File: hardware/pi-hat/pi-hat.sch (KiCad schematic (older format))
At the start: 75 parts, among them J1 PWR IN, J10 6-8, J11 PWM0, J12 PWM1, J13 KLPX-0848A-2-B, J14 KLPX-0848A-2-R, J2 A-F, J3 40HAT, J4 G-M, J5 N-Q, J6 PANEL_PWR, J7 PANEL_CTL, J8 2-5, J9 WP, Q1 DMG2305UX, Q2 DMMT5401, Q3 DMN6075S, Q4 NTR4171P, U1 CAT24C32, U10 L78L33_SOT89, U11 L78L33_SOT89, U12 PCM5122PW, U2 CM1293A, U3 CM1293A, U4 CM1293A, U5 CM1293A, U6 CM1293A, U7 CM1293A, U8 MCP23S17_SO, U9 MCP23S17_SO

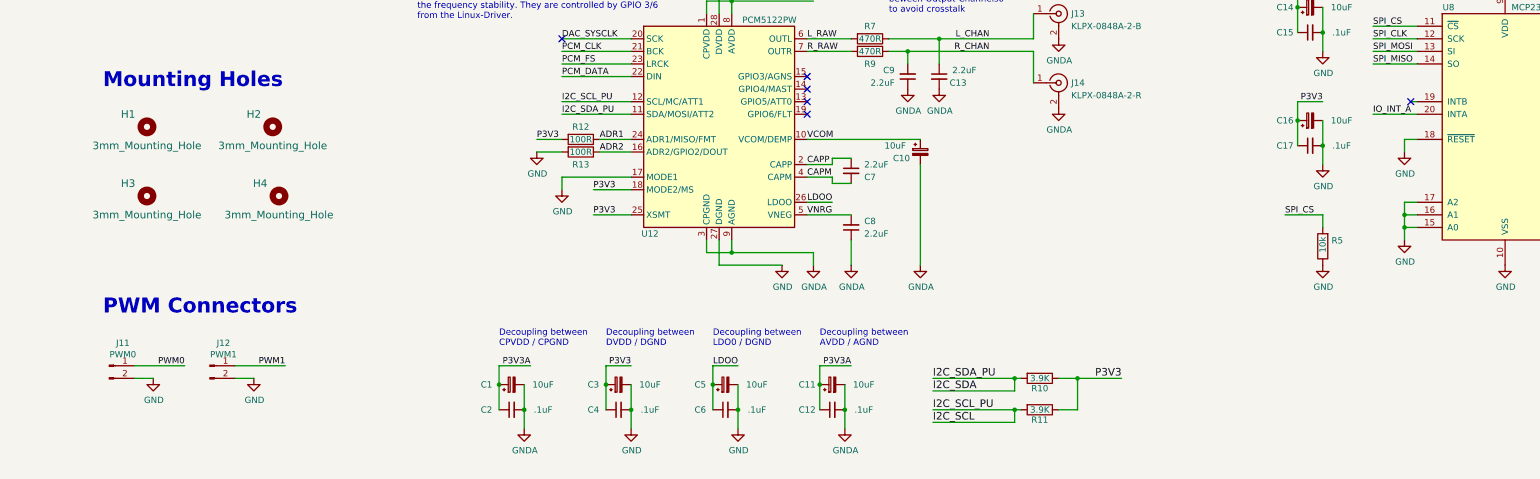
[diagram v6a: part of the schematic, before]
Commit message: fully routed
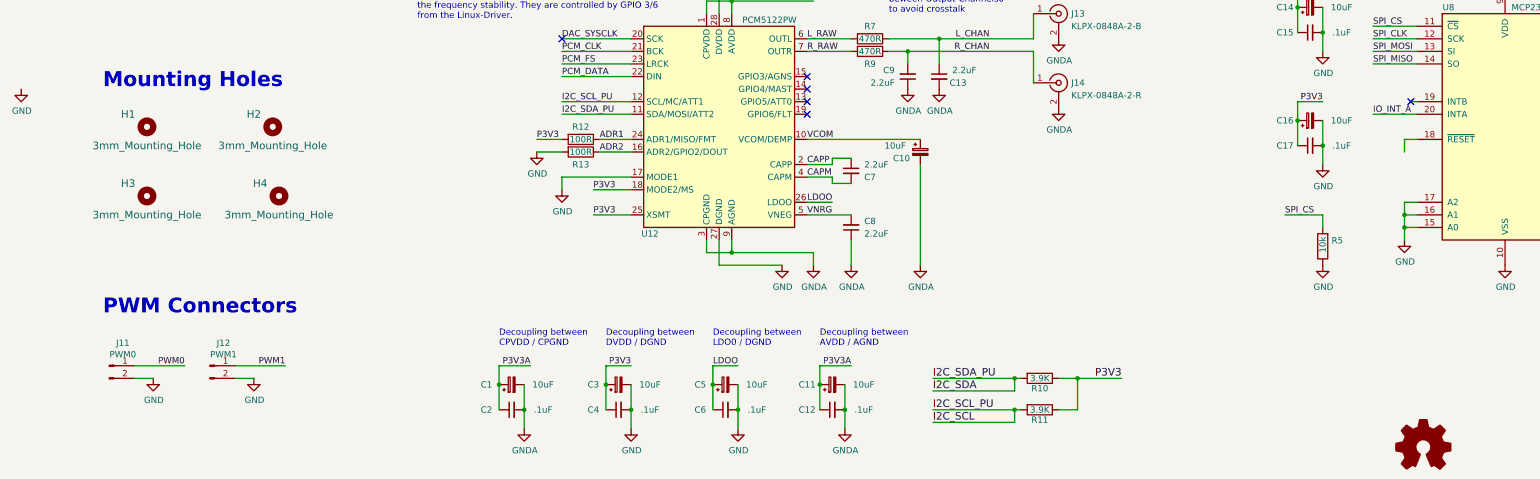
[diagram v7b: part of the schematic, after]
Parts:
- JP1: footprint Jumper:SolderJumper-2_P1.3mm_Bridged2Bar_RoundedPad1.0x1.5mm -> NetTie:NetTie-2_SMD_Pad0.5mm
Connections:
- net GND: no longer U8.18 (~RESET~)
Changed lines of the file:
@@
 L power:GND #PWR018
 U 1 1 5ED9D663
-P 11400 8650
-F 0 "#PWR018" H 11400 8400 50  0001 C CNN
-F 1 "GND" H 11405 8477 50  0000 C CNN
-F 2 "" H 11400 8650 50  0001 C CNN
-F 3 "" H 11400 8650 50  0001 C CNN
-	1    11400 8650
+P 400 8150
+F 0 "#PWR018" H 400 7900 50  0001 C CNN
+F 1 "GND" H 405 7977 50  0000 C CNN
+F 2 "" H 400 8150 50  0001 C CNN
+F 3 "" H 400 8150 50  0001 C CNN
+	1    400  8150
 	1    0    0    -1
 $EndComp
@@
 F 0 "JP1" H 9250 4421 50  0001 C CNN
 F 1 "Jumper_NC_Small" H 9250 4421 50  0001 C CNN
-F 2 "Jumper:SolderJumper-2_P1.3mm_Bridged2Bar_RoundedPad1.0x1.5mm" H 9250 4300 50  0001 C CNN
+F 2 "NetTie:NetTie-2_SMD_Pad0.5mm" H 9250 4300 50  0001 C CNN
 F 3 "~" H 9250 4300 50  0001 C CNN
 	1    9250 4300
@@
 	12550 2300 14800 2300
 Connection ~ 12550 2500
+$Comp
+L Graphic:Logo_Open_Hardware_Small #LOGO1
+U 1 1 5E8DC3DA
+P 11550 11000
+F 0 "#LOGO1" H 11550 11500 50  0001 C CNN
+F 1 "Logo_Open_Hardware_Large" H 11550 10600 50  0001 C CNN
+F 2 "Symbol:OSHW-Logo2_7.3x6mm_SilkScreen" H 11550 11000 50  0001 C CNN
+F 3 "~" H 11550 11000 50  0001 C CNN
+	1    11550 11000
+	1    0    0    -1
+$EndComp
 $EndSCHEMATC

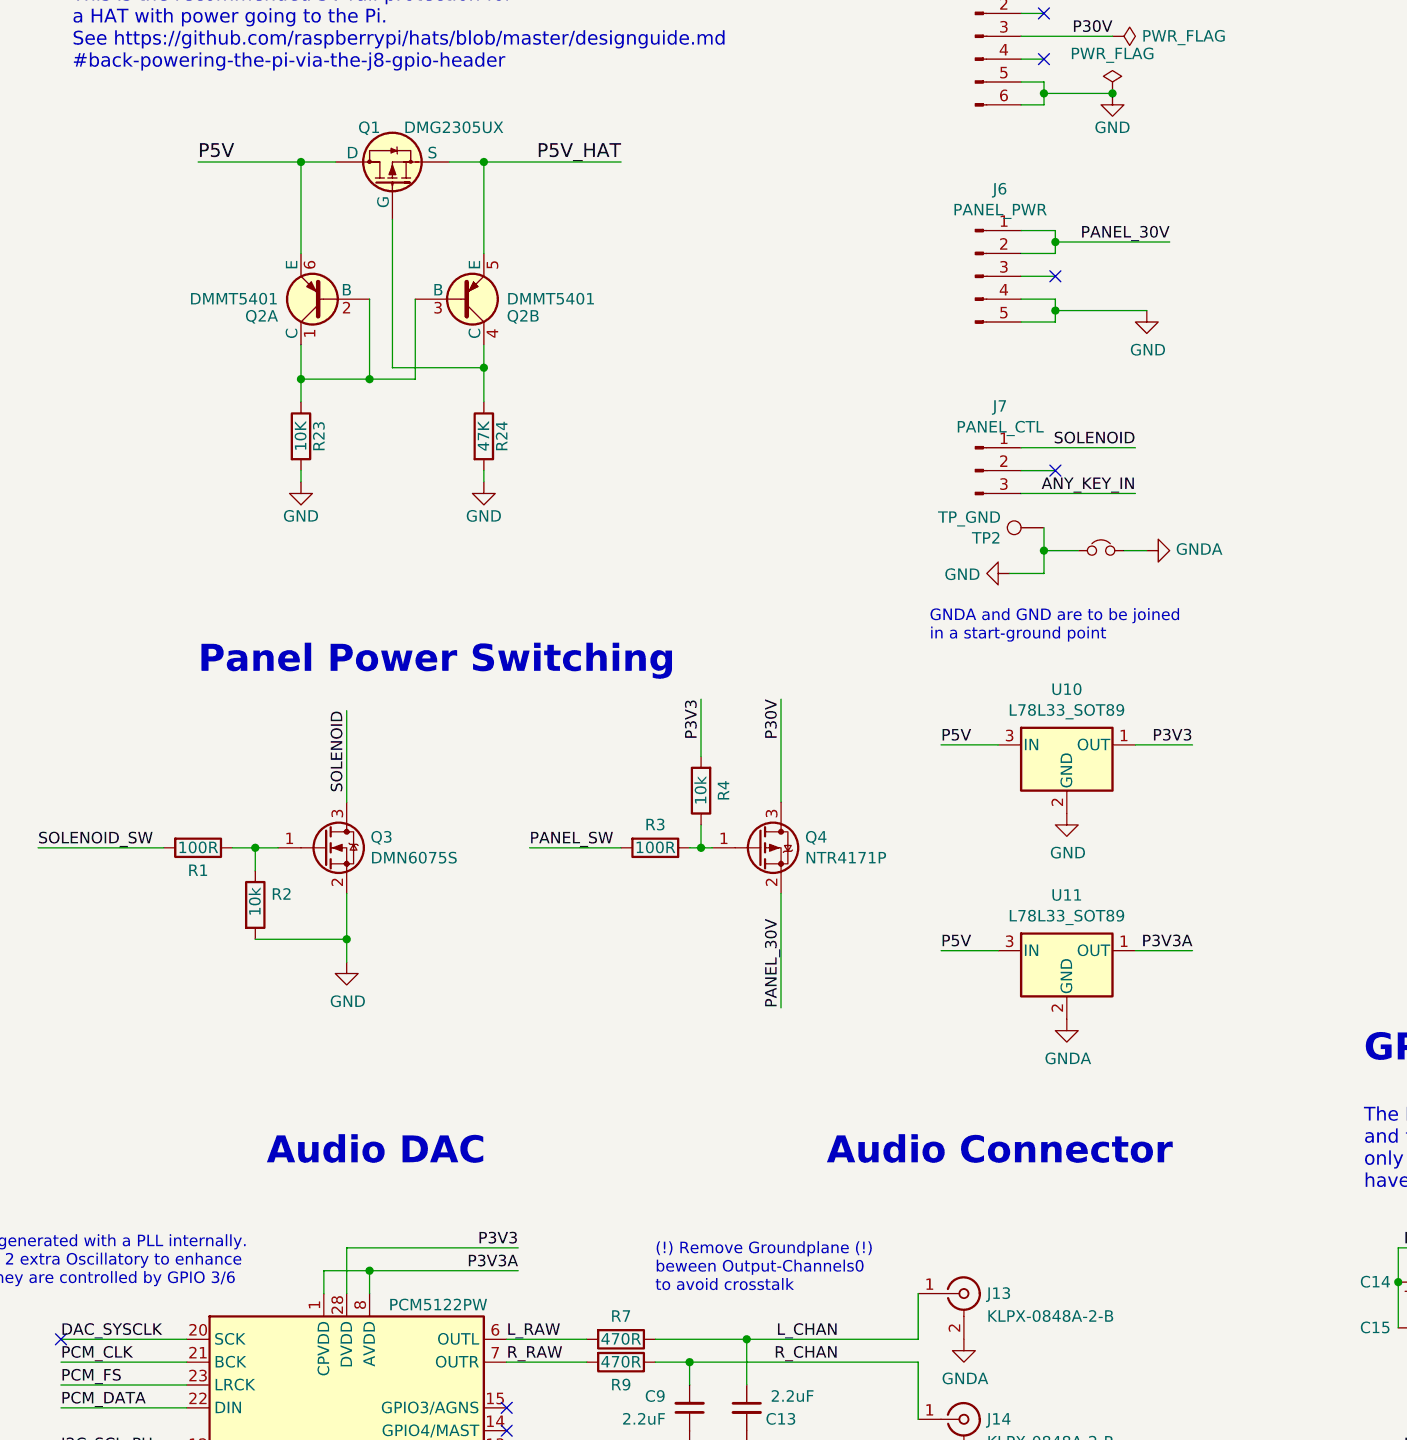
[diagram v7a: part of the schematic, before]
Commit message: add icons and voltage testpoints
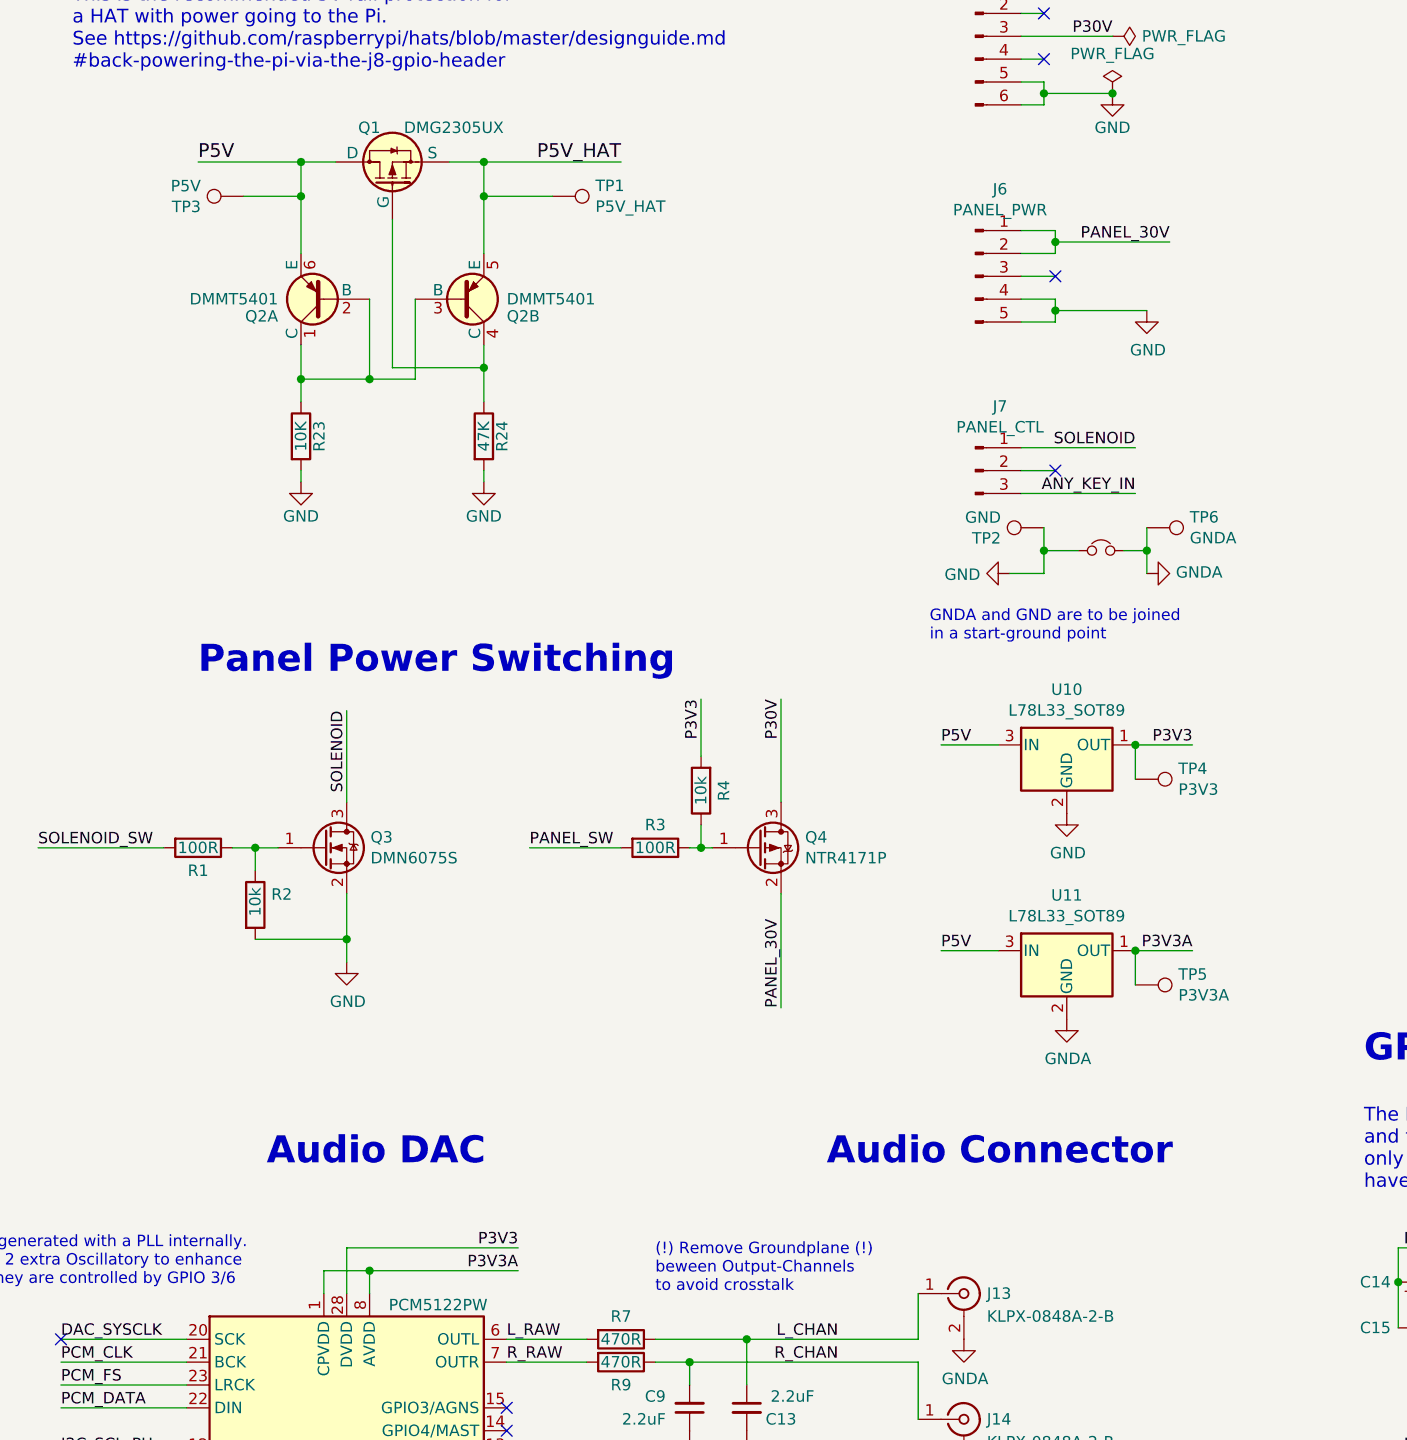
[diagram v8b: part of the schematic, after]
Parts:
- added OSHW1: Logo_Open_Hardware_Large, Symbol:OSHW-Logo2_7.3x6mm_SilkScreen, symbol Graphic:Logo_Open_Hardware_Small
- added TP1: P5V_HAT, TestPoint:TestPoint_Pad_D2.0mm, symbol Connector:TestPoint
- added TP3: P5V, TestPoint:TestPoint_Pad_D2.0mm, symbol Connector:TestPoint
- added TP4: P3V3, TestPoint:TestPoint_Pad_D2.0mm, symbol Connector:TestPoint
- added TP5: P3V3A, TestPoint:TestPoint_Pad_D2.0mm, symbol Connector:TestPoint
- added TP6: GNDA, TestPoint:TestPoint_Pad_D2.0mm, symbol Connector:TestPoint
- TP2: value TP_GND -> GND
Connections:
- net GNDA: now also TP6.1
- net P3V3: now also TP4.1
- net P3V3A: now also TP5.1
- net P5V: now also TP3.1
- net P5V_HAT: now also TP1.1
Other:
- note added: "(!) Remove Groundplane (!)\nbeween Output-Channels\nto avoid crosstalk"
- note removed: "(!) Remove Groundplane (!)\nbeween Output-Channels0\nto avoid crosstalk"
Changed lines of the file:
@@
 $EndComp
-Wire Wire Line
-	8900 1850 9300 1850
 Wire Wire Line
 	8900 1950 9000 1950
@@
 Connection ~ 6550 2600
 Wire Wire Line
-	6550 3000 6550 2600
+	6550 3000 6550 2750
 Connection ~ 5750 2600
 Wire Wire Line
-	5750 3000 5750 2600
+	5750 3000 5750 2750
 Connection ~ 6050 3550
 Wire Wire Line
@@
 P 9000 4200
 F 0 "TP2" V 8954 4388 50  0000 L CNN
-F 1 "TP_GND" V 9045 4388 50  0000 L CNN
+F 1 "GND" V 9045 4388 50  0000 L CNN
 F 2 "TestPoint:TestPoint_Pad_D2.0mm" H 9200 4200 50  0001 C CNN
 F 3 "~" H 9200 4200 50  0001 C CNN
@@
 L power:GNDA #PWR0106
 U 1 1 6024E074
-P 9450 4300
-F 0 "#PWR0106" H 9450 4050 50  0001 C CNN
-F 1 "GNDA" V 9455 4173 50  0000 R CNN
-F 2 "" H 9450 4300 50  0001 C CNN
-F 3 "" H 9450 4300 50  0001 C CNN
-	1    9450 4300
+P 9450 4400
+F 0 "#PWR0106" H 9450 4150 50  0001 C CNN
+F 1 "GNDA" V 9455 4273 50  0000 R CNN
+F 2 "" H 9450 4400 50  0001 C CNN
+F 3 "" H 9450 4400 50  0001 C CNN
+	1    9450 4400
 	0    -1   -1   0
 $EndComp
@@
 $EndComp
 Text Notes 7300 7550 0    50   ~ 0
-(!) Remove Groundplane (!)\nbeween Output-Channels0\nto avoid crosstalk
+(!) Remove Groundplane (!)\nbeween Output-Channels\nto avoid crosstalk
 Wire Wire Line
 	10750 9250 10750 9150
@@
 Connection ~ 12550 2500
 $Comp
-L Graphic:Logo_Open_Hardware_Small #LOGO1
+L Graphic:Logo_Open_Hardware_Small OSHW1
 U 1 1 5E8DC3DA
 P 11550 11000
-F 0 "#LOGO1" H 11550 11500 50  0001 C CNN
+F 0 "OSHW1" H 11550 11500 50  0001 C CNN
 F 1 "Logo_Open_Hardware_Large" H 11550 10600 50  0001 C CNN
 F 2 "Symbol:OSHW-Logo2_7.3x6mm_SilkScreen" H 11550 11000 50  0001 C CNN
@@
 	1    0    0    -1
 $EndComp
+$Comp
+L Connector:TestPoint TP3
+U 1 1 5EA57104
+P 5500 2750
+F 0 "TP3" V 5454 2938 50  0000 L CNN
+F 1 "P5V" V 5545 2938 50  0000 L CNN
+F 2 "TestPoint:TestPoint_Pad_D2.0mm" H 5700 2750 50  0001 C CNN
+F 3 "~" H 5700 2750 50  0001 C CNN
+	1    5500 2750
+	0    -1   -1   0
+$EndComp
+$Comp
+L Connector:TestPoint TP1
+U 1 1 5EA97686
+P 6850 2750
+F 0 "TP1" V 6804 2938 50  0000 L CNN
+F 1 "P5V_HAT" V 6895 2938 50  0000 L CNN
+F 2 "TestPoint:TestPoint_Pad_D2.0mm" H 7050 2750 50  0001 C CNN
+F 3 "~" H 7050 2750 50  0001 C CNN
+	1    6850 2750
+	0    1    1    0
+$EndComp
+Wire Wire Line
+	6850 2750 6550 2750
+Connection ~ 6550 2750
+Wire Wire Line
+	6550 2750 6550 2600
+$Comp
+L Connector:TestPoint TP4
+U 1 1 5EACB533
+P 9400 5300
+F 0 "TP4" V 9354 5488 50  0000 L CNN
+F 1 "P3V3" V 9445 5488 50  0000 L CNN
+F 2 "TestPoint:TestPoint_Pad_D2.0mm" H 9600 5300 50  0001 C CNN
+F 3 "~" H 9600 5300 50  0001 C CNN
+	1    9400 5300
+	0    1    1    0
+$EndComp
+$Comp
+L Connector:TestPoint TP5
+U 1 1 5EACDD2D
+P 9400 6200
+F 0 "TP5" V 9354 6388 50  0000 L CNN
+F 1 "P3V3A" V 9445 6388 50  0000 L CNN
+F 2 "TestPoint:TestPoint_Pad_D2.0mm" H 9600 6200 50  0001 C CNN
+F 3 "~" H 9600 6200 50  0001 C CNN
+	1    9400 6200
+	0    1    1    0
+$EndComp
+Wire Wire Line
+	9400 6200 9400 6050
+Connection ~ 9400 6050
+Wire Wire Line
+	9400 5300 9400 5150
+Connection ~ 9400 5150
+$Comp
+L Connector:TestPoint TP6
+U 1 1 5EB41904
+P 9450 4200
+F 0 "TP6" V 9404 4388 50  0000 L CNN
+F 1 "GNDA" V 9495 4388 50  0000 L CNN
+F 2 "TestPoint:TestPoint_Pad_D2.0mm" H 9650 4200 50  0001 C CNN
+F 3 "~" H 9650 4200 50  0001 C CNN
+	1    9450 4200
+	0    1    1    0
+$EndComp
+Wire Wire Line
+	9450 4200 9450 4300
+Wire Wire Line
+	9450 4300 9450 4400
+Connection ~ 9450 4300
+Wire Wire Line
+	8900 1850 9300 1850
+Wire Wire Line
+	5500 2750 5750 2750
+Connection ~ 5750 2750
+Wire Wire Line
+	5750 2750 5750 2600
 $EndSCHEMATC
